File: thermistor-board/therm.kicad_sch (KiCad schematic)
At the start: 12 parts, among them J1 Conn_01x06_Pin, J10 Conn_01x06_Pin, J18 Conn_01x06_Pin, J5 Conn_01x06_Pin

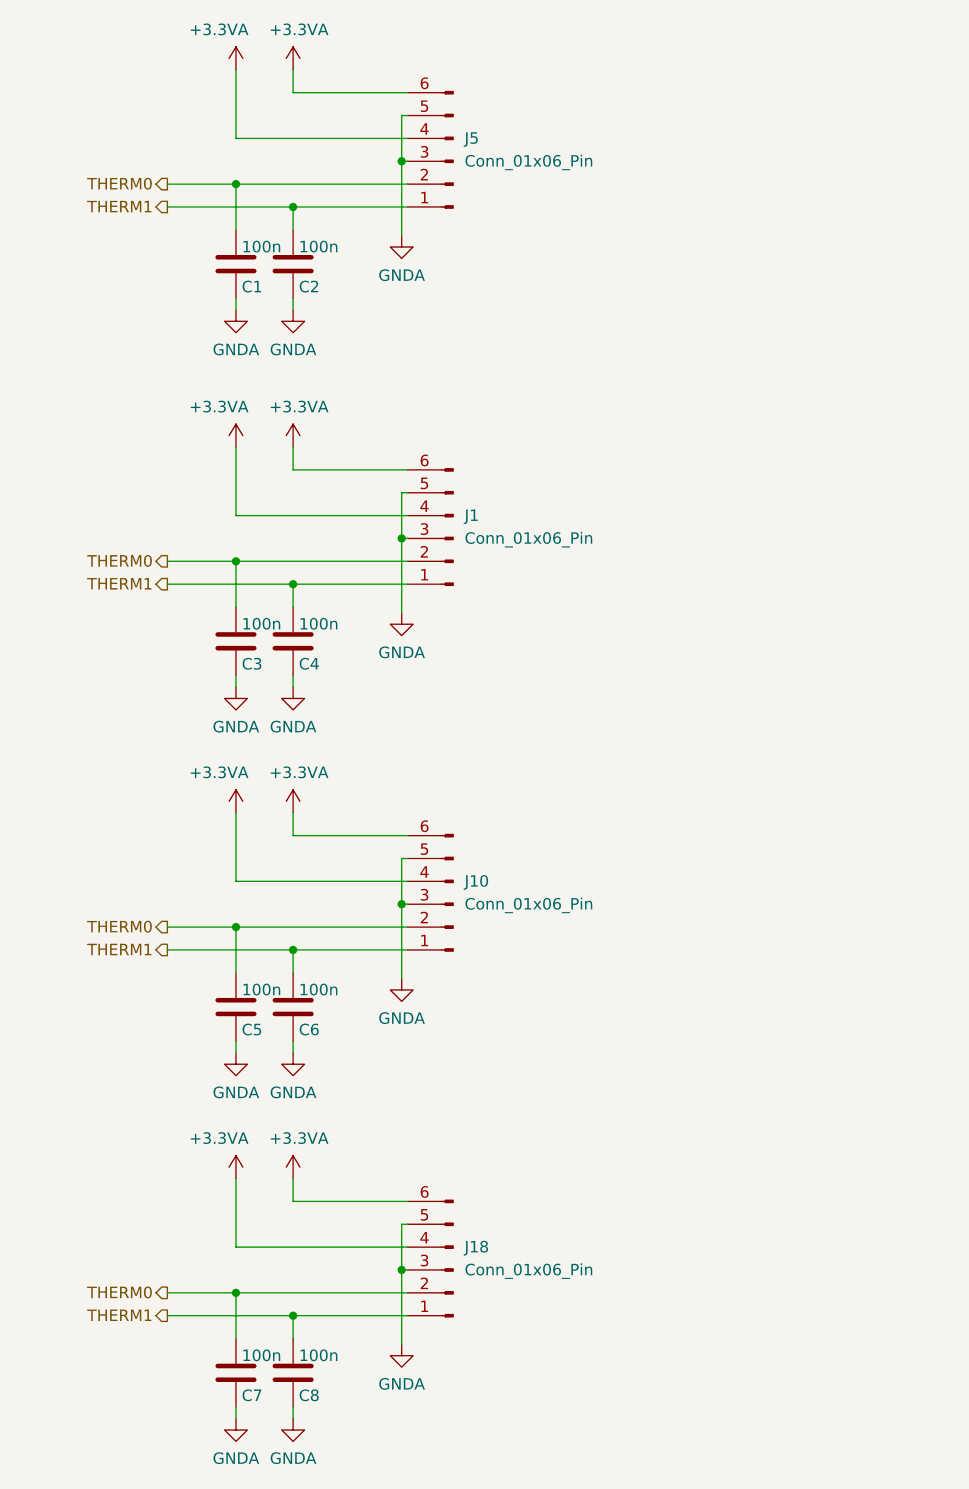
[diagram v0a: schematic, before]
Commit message: temp update
To find GND issue
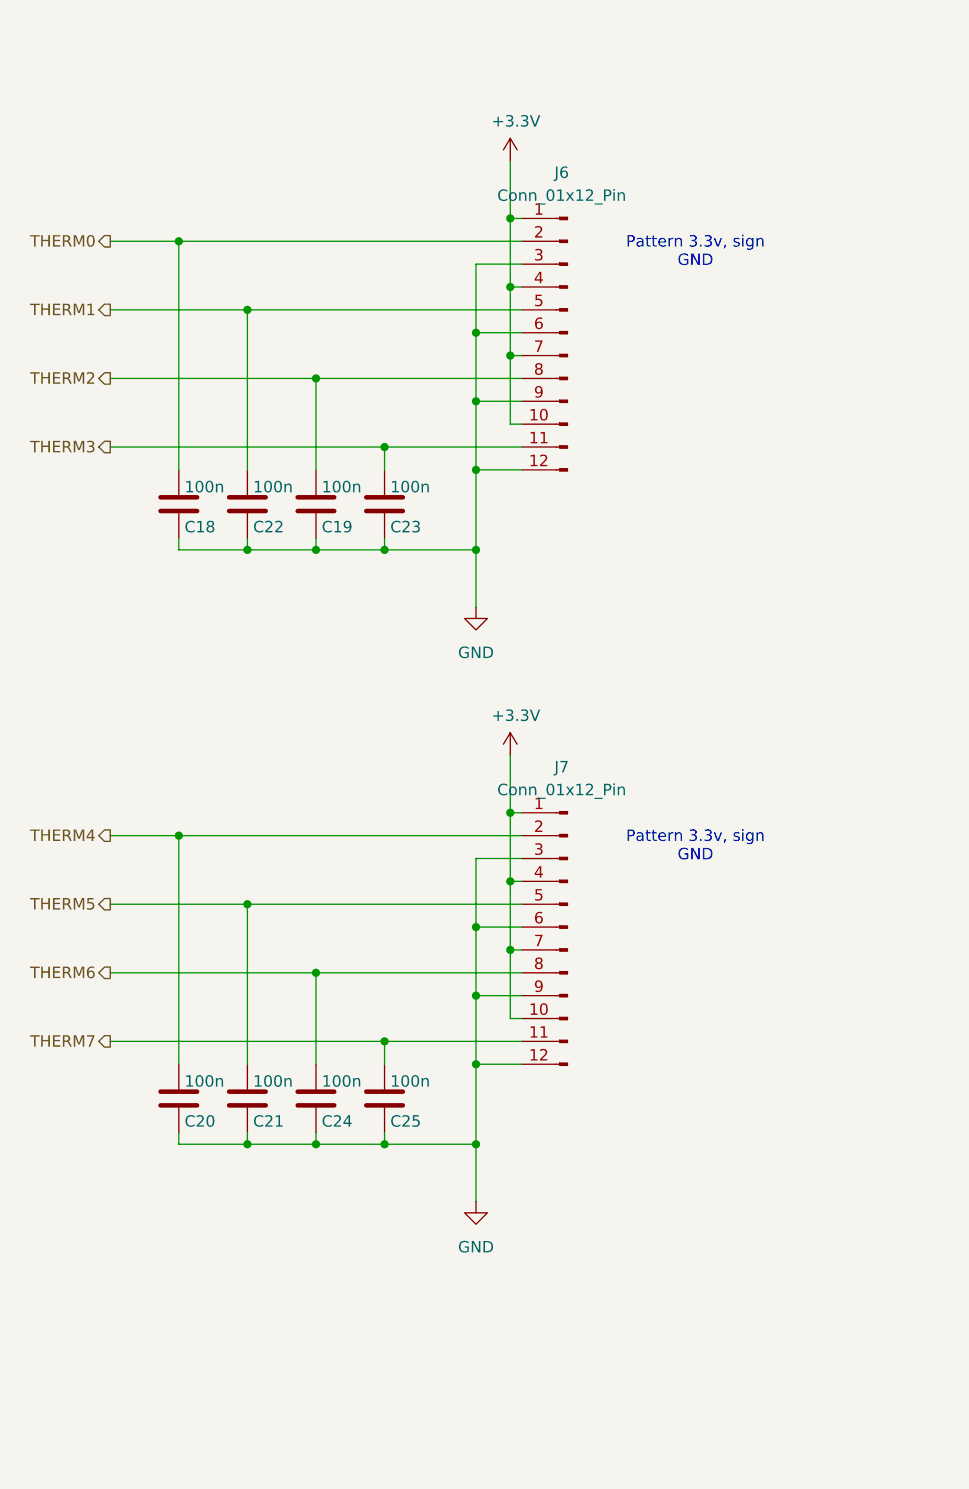
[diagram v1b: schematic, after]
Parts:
- removed C5, C6, C7, C8: 100n, Capacitor_SMD:C_0805_2012Metric_Pad1.18x1.45mm_HandSolder, symbol Device:C
- removed J1, J10, J18, J5: Conn_01x06_Pin, symbol Connector:Conn_01x06_Pin
- added C20, C21, C24, C25: 100n, Capacitor_SMD:C_0805_2012Metric_Pad1.18x1.45mm_HandSolder, symbol Device:C
- added J6, J7: Conn_01x12_Pin, Connector_Molex:Molex_Micro-Fit_3.0_43045-1200_2x06_P3.00mm_Horizontal, symbol Connector:Conn_01x12_Pin
- renumbered C1 to C18, C3 to C19, C2 to C22, C4 to C23
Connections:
- net THERM0: now also J6.2 (Pin_2); no longer C19.1
- net THERM1: now also J6.5 (Pin_5); no longer C23.1
- net GNDA renamed GND
- net GND: now also C20.2, C21.2, C24.2, C25.2, J6.12 (Pin_12), J6.3 (Pin_3), J6.6 (Pin_6), J6.9 (Pin_9), J7.12 (Pin_12), J7.3 (Pin_3), J7.6 (Pin_6), J7.9 (Pin_9)
- new net +3.3V: J6.1 (Pin_1), J6.10 (Pin_10), J6.4 (Pin_4), J6.7 (Pin_7), J7.1 (Pin_1), J7.10 (Pin_10), J7.4 (Pin_4), J7.7 (Pin_7)
- new net THERM2: C19.1, J6.8 (Pin_8)
- new net THERM3: C23.1, J6.11 (Pin_11)
- new net THERM4: C20.1, J7.2 (Pin_2)
- new net THERM5: C21.1, J7.5 (Pin_5)
- new net THERM6: C24.1, J7.8 (Pin_8)
- new net THERM7: C25.1, J7.11 (Pin_11)
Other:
- note added: "Pattern 3.3v, sign GND"
- moved on the sheet: C18, C19, C22, C23

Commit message: Add fuses and update connector/capacitor references
Added Device: Fuse symbols and instances to the schematic for overcurrent protection. Updated connector and capacitor reference designators and locations, and extended several nets to new connectors and components for improved organization and safety.
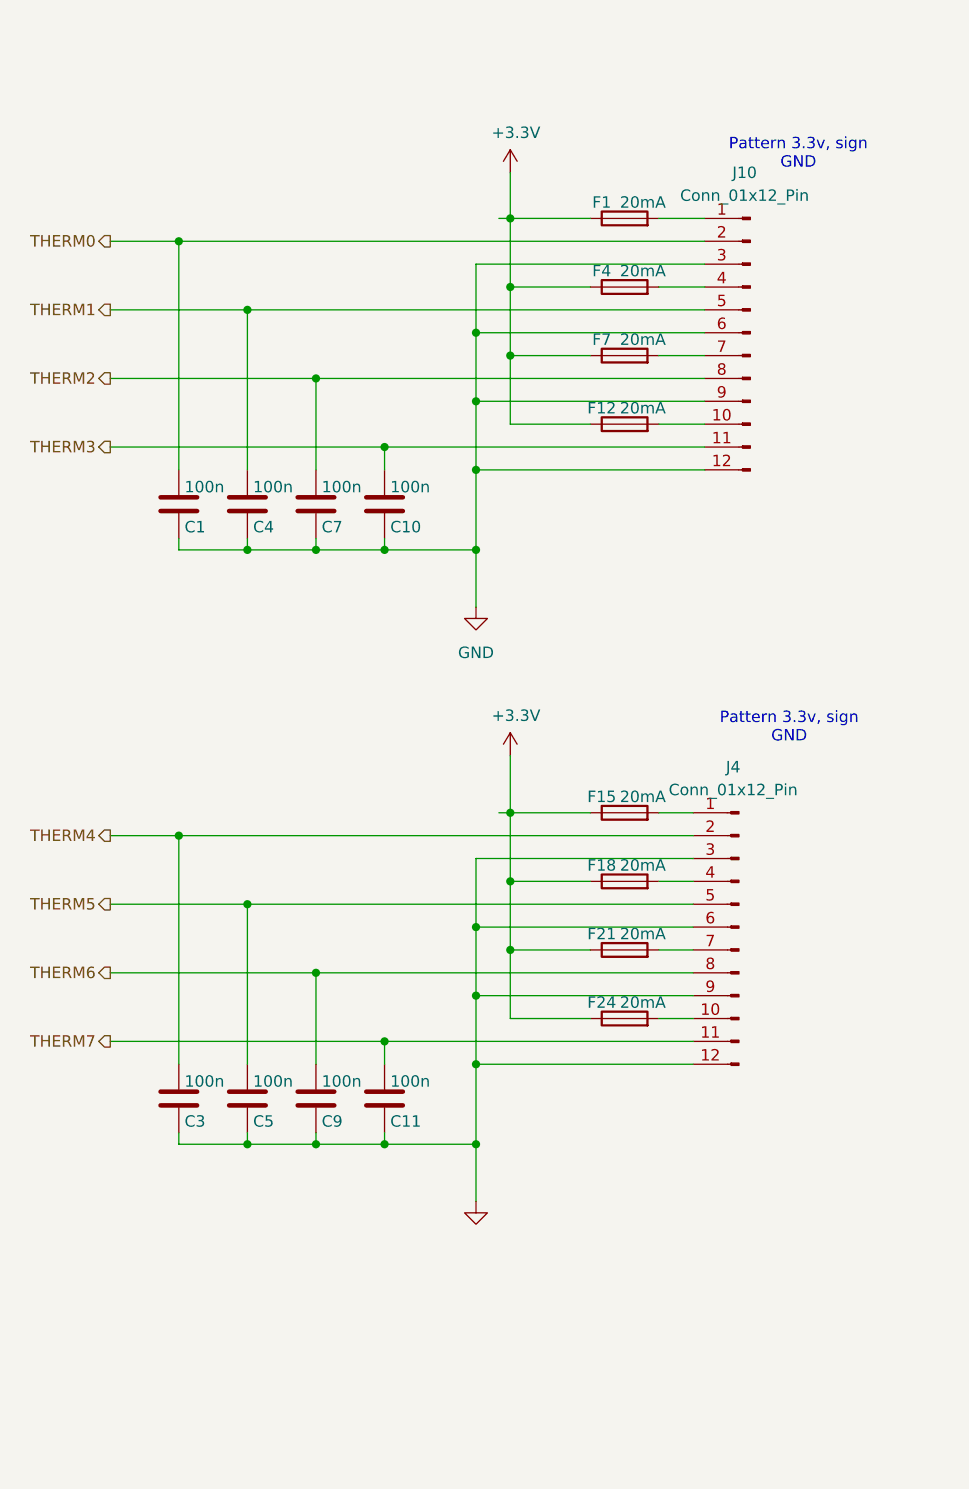
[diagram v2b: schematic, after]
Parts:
- added F1, F12, F15, F18, F21, F24, F4, F7: 20mA, Fuse:Fuse_0805_2012Metric_Pad1.15x1.40mm_HandSolder, symbol Device:Fuse
- renumbered C18 to C1, C23 to C10, C25 to C11, C20 to C3, C22 to C4, C21 to C5, C19 to C7, C24 to C9, J6 to J10, J7 to J4
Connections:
- net +3.3V: now also F1.1, F12.1, F15.1, F18.1, F21.1, F24.1, F4.1, F7.1; no longer J10.1 (Pin_1), J10.10 (Pin_10), J10.4 (Pin_4), J10.7 (Pin_7), J4.1 (Pin_1), J4.10 (Pin_10), J4.4 (Pin_4), J4.7 (Pin_7)
- new net: F1.2, J10.1 (Pin_1)
- new net: F12.2, J10.10 (Pin_10)
- new net: F4.2, J10.4 (Pin_4)
- new net: F7.2, J10.7 (Pin_7)
- new net: F18.2, J4.4 (Pin_4)
- new net: F24.2, J4.10 (Pin_10)
- new net: F15.2, J4.1 (Pin_1)
- new net: F21.2, J4.7 (Pin_7)
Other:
- moved on the sheet: J10, J4

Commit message: Add clamped_div schematic and update symbols/libs
Add a new clamped_div.kicad_sch implementing a voltage divider/clamped input (optional zener diodes, resistor network and notes). Update therm.kicad_sch to include a project title block and add an ESD protection diode symbol (PESD3V3L4UW) and related symbol data. Update sym-lib-table to add XAL6030 and Molex Microfit symbol libraries. Remove the now-unused tem.kicad_sch template. These changes add the clamped divider design and ensure required symbol libraries are available.
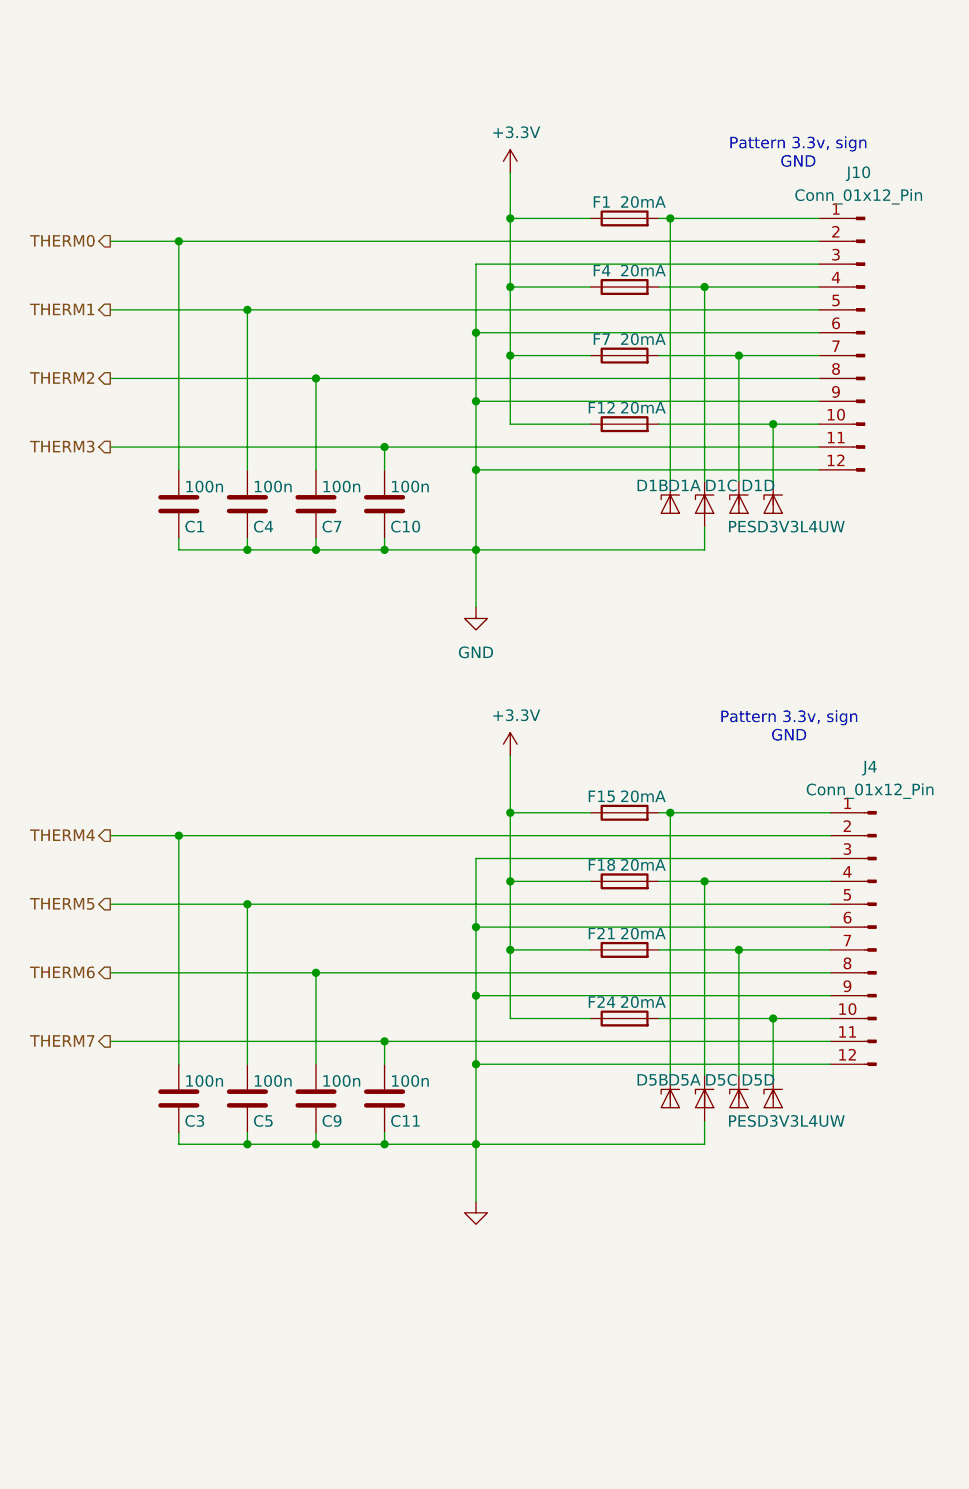
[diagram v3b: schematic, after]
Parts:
- added D1, D5: PESD3V3L4UW, Package_TO_SOT_SMD:SOT-665, symbol Power_Protection:PESD3V3L4UW
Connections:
- net GND: now also D1.2 (A), D5.2 (A)
- net at F1.2, J10.1 (Pin_1): now also D1.3 (K2)
- net at F12.2, J10.10 (Pin_10): now also D1.5 (K4)
- net at F4.2, J10.4 (Pin_4): now also D1.1 (K1)
- net at F7.2, J10.7 (Pin_7): now also D1.4 (K3)
- net at F18.2, J4.4 (Pin_4): now also D5.1 (K1)
- net at F24.2, J4.10 (Pin_10): now also D5.5 (K4)
- net at F15.2, J4.1 (Pin_1): now also D5.3 (K2)
- net at F21.2, J4.7 (Pin_7): now also D5.4 (K3)
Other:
- company: (none) -> SUFST
- title: (none) -> Can-Node
- moved on the sheet: J10, J4
